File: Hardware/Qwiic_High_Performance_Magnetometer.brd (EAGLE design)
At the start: 25.4 x 25.4 mm, 46 parts, among them J1 Qwiic, J2 Qwiic, U1 MMC5893MA_QFN16

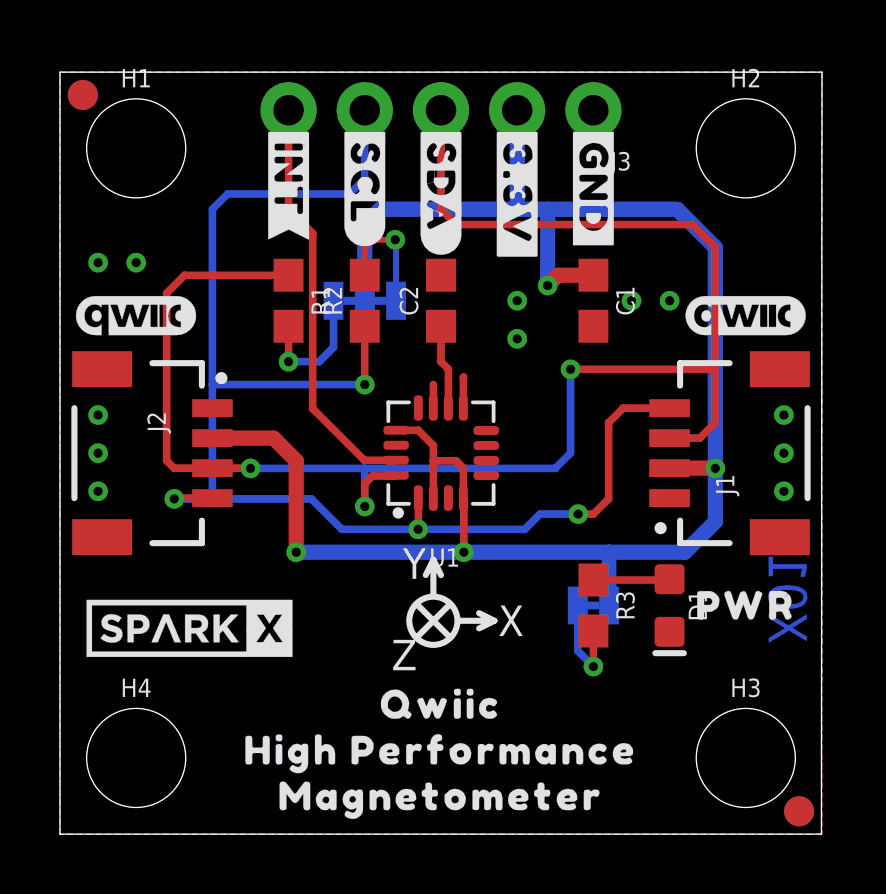
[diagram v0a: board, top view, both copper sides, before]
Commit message: Added SPI breakout header; created PCB production files.
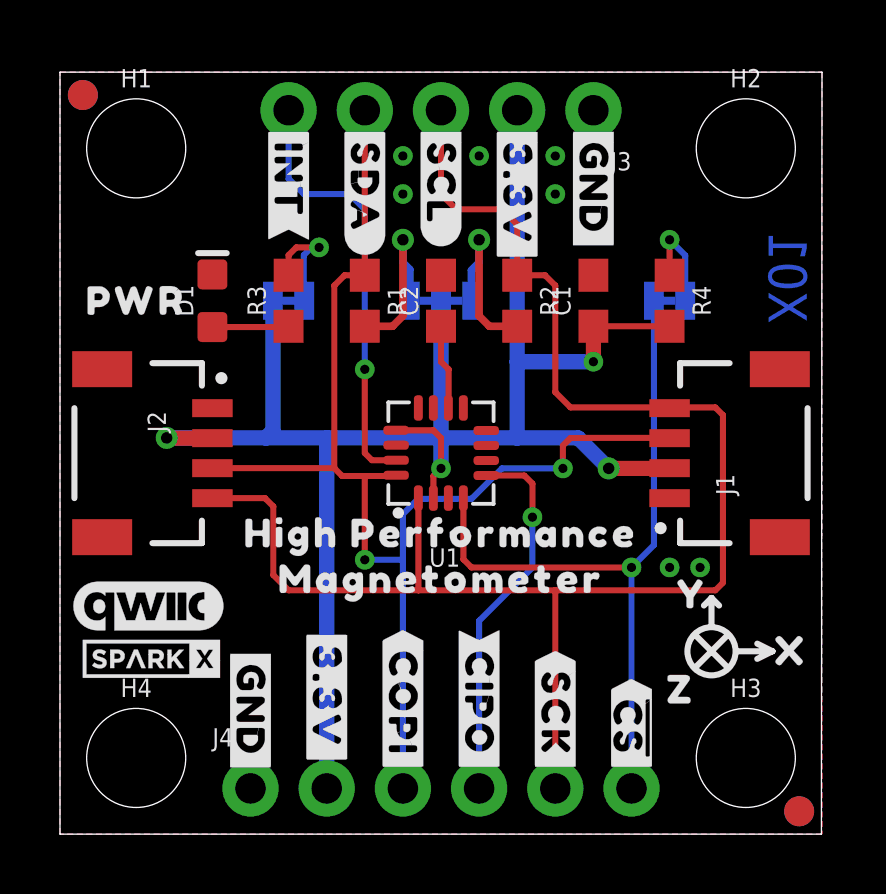
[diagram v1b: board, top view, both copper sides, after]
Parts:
- added J4: (no value), SparkFun-Connectors:1X06_NO_SILK
- added JP2: JUMPER-SMT_2_NC_TRACE_SILK, SparkFun-Jumpers:SMT-JUMPER_2_NC_TRACE_SILK
- added R4: 10k, SparkFun-Resistors:0603
- added U$23: (no value), output:#SPI#9
- added U$24: (no value), output:MAGNETOMETER12
- added U$25: (no value), output:X15
- added U$26: (no value), output:Y16
- added U$27, U$39: (no value), output:Z17
- added U$28: (no value), output:#GND#4
- added U$29: (no value), output:#3#3V#0
- added U$30: (no value), output:#COPI#12
- added U$31: (no value), output:#CIPO#11
- added U$32: (no value), output:#SCK#13
- added U$33: (no value), output:##CS##10
- added U$34: (no value), output:MADE_IN_THE_USA20
- added U$35: (no value), output:#SCL#6
- added U$36: SPARKX-LOGO2, SparkX:SPARKX-TINY
- added U$37: SPARKX-LOGO3, SparkX:SPARKX-SMALL
- added U$38: (no value), output:#SDA#5
- LOGO2, LOGO3: value QWIIC_LOGO_4MM -> QWIIC_LOGO_5MM; device SparkFun-Aesthetics:QWIIC_4MM -> SparkFun-Aesthetics:QWIIC_5MM
- U$1: value SPARKX-LOGO5 -> (none); device SparkX:SPARKX-LARGE -> output:HIGH_PERFORMANCE11
- U$14: device output:#SCL#6 -> output:#SCK#13
- U$15: device output:#SDA#5 -> output:##CS##10
- U$17: device output:MADE_IN_THE_USA13 -> output:#GND#4
- U$18: device output:QWIIC10 -> output:#3#3V#0
- U$19: device output:HIGH_PERFORMANCE11 -> output:Y16
- U$2: value SPARKX-LOGO3 -> (none); device SparkX:SPARKX-SMALL -> output:#SCL#6
- U$20: device output:MAGNETOMETER12 -> output:X15
- U$5: device output:#SCL#6 -> output:#SDA#5
- U$6: device output:#SDA#5 -> output:#CIPO#11
- U$9: device output:QWIIC10 -> output:#COPI#12
- moved U$14 22.7 mm to (16.5, 1.91), flipped to the top
- moved U$15 22.7 mm to (19.1, 1.91), flipped to the top
- moved U$8 22.7 mm to (2.54, 17.8)
- moved LOGO2 22.0 mm to (3.05, 7.62), flipped to the bottom
- moved U$6 21.9 mm to (14.0, 1.91)
- moved U$2 18.9 mm to (12.7, 23.7), turned to 270 degrees
- moved D1 18.3 mm to (5.08, 17.8), turned to 90 degrees
- moved JP3 14.4 mm to (7.62, 17.8), turned to 0 degrees
- moved R3 14.4 mm to (7.62, 17.8), turned to 90 degrees
- moved U$21 12.1 mm to (7.62, 16.0)
- moved U$20 12.1 mm to (24.4, 6.10), flipped to the top
- moved LOGO3 9.66 mm to (2.92, 7.62)
- moved U$19 9.16 mm to (21.1, 8.00), flipped to the top
- moved U$17 8.29 mm to (6.35, 6.35), flipped to the top, turned to 270 degrees
- moved U$11 7.24 mm to (12.7, 8.51)
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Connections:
- removed net SCL: J1.4, J2.4, J3.4, R2.1, U1.1
- removed net SDA: J1.3, J2.3, J3.3, R1.1, U1.16
- new net !CS!: J4.6, JP2.1, U1.4
- new net CIPO: J4.4, U1.5
- new net N$5: JP2.2, R4.1
- new net SCL/SCK: J1.4, J2.4, J3.3, J4.5, R2.1, U1.1
- new net SDA/COPI: J1.3, J2.3, J3.4, J4.3, R1.1, U1.16
- net 3.3V: now also J4.2, R4.2; no longer U1.4
- net GND: now also J4.1
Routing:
- net SDA: track 55.0 -> 0.00 mm, vias 3 -> 0
- net SCL/SCK: track 0.00 -> 53.4 mm
- net SCL: track 46.9 -> 0.00 mm, vias 4 -> 0
- net SDA/COPI: track 0.00 -> 42.6 mm, vias 0 -> 2
- net !CS!: track 0.00 -> 24.3 mm, vias 0 -> 1
- net CIPO: track 0.00 -> 12.5 mm, vias 0 -> 1
- net N$5: track 0.00 -> 3.43 mm, vias 0 -> 1
- net N$2: track 4.09 -> 6.10 mm
- net GND: track 1.82 -> 0.00 mm, vias 12 -> 7
- net N$3: track 4.43 -> 6.08 mm
- net 3.3V: track 62.6 -> 61.6 mm
- net INT: track 13.8 -> 14.5 mm, vias 0 -> 1
- net N$1: track 3.43 -> 3.94 mm
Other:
- board text removed: "X"
- board text removed: "Y"
- board text removed: "Z"

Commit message: Fixed SPI header alignment.
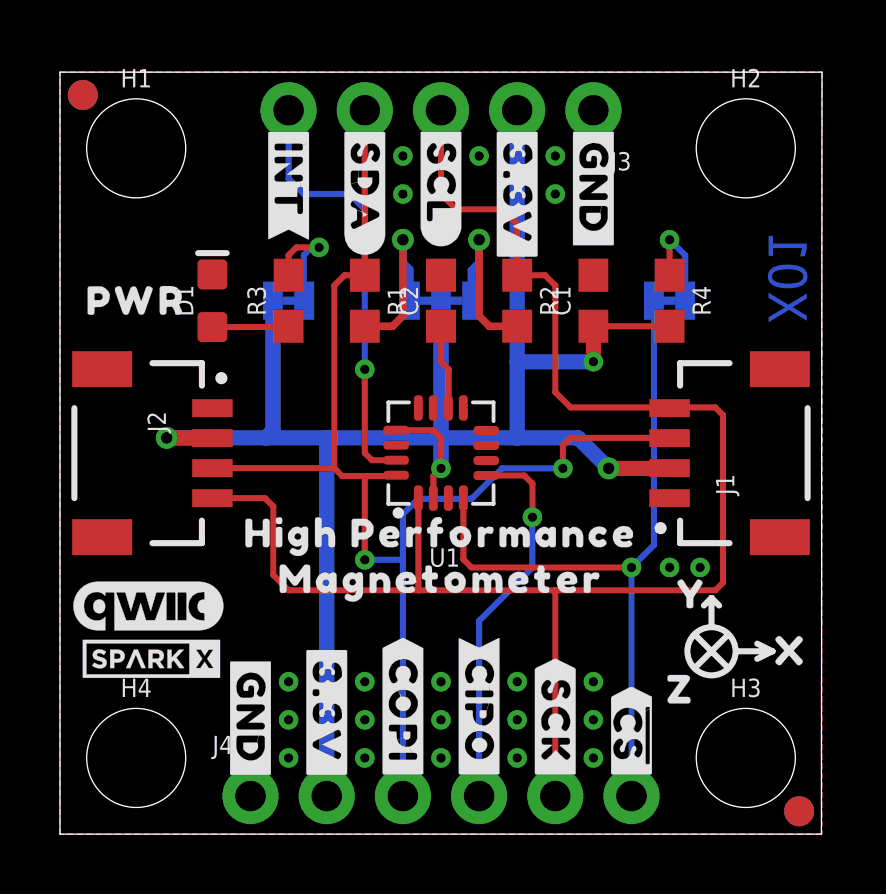
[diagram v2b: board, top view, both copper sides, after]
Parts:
- moved U$18 0.51 mm to (8.89, 6.48)
- moved J4 0.25 mm to (6.35, 1.27)
- moved U$14 0.25 mm to (16.5, 1.65)
- moved U$15 0.25 mm to (19.1, 1.65)
- moved U$30 0.25 mm to (11.4, 1.65)
- moved U$31 0.25 mm to (14.0, 1.65)
- moved U$32 0.25 mm to (16.5, 1.65)
- moved U$33 0.25 mm to (19.1, 1.65)
- moved U$6 0.25 mm to (14.0, 1.65)
- moved U$9 0.25 mm to (11.4, 1.65)
- moved U$17 0.25 mm to (6.35, 6.10)
- moved U$28 0.25 mm to (6.35, 6.10)
- moved U$29 0.25 mm to (8.89, 6.48)

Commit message: Improved top ground plane under the IC.
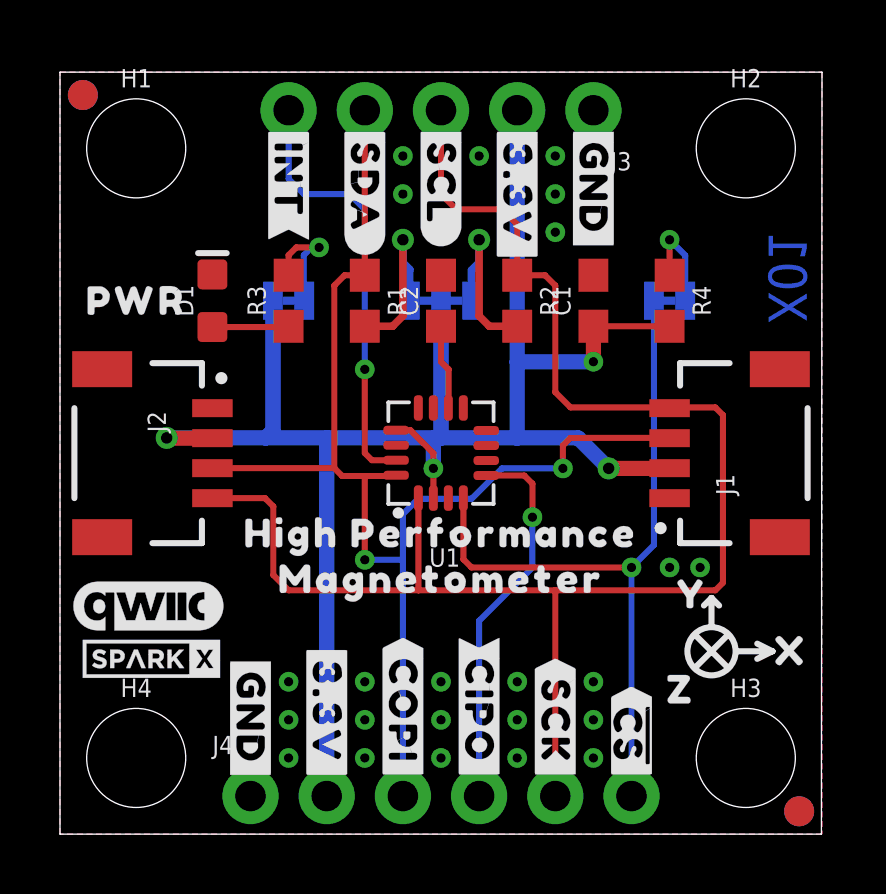
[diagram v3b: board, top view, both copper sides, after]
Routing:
- net 3.3V: track 61.8 -> 61.2 mm
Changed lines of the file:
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@@
 <drawing>
 <settings>
-<setting alwaysvectorfont="yes"/>
+<setting alwaysvectorfont="no"/>
 <setting verticaltext="up"/>
 </settings>
-<grid distance="0.05" unitdist="inch" unit="inch" style="lines" multiple="1" display="yes" altdistance="0.005" altunitdist="inch" altunit="inch"/>
+<grid distance="0.01" unitdist="inch" unit="inch" style="lines" multiple="1" display="yes" altdistance="0.005" altunitdist="inch" altunit="inch"/>
 <layers>
 <layer number="1" name="Top" color="4" fill="1" visible="yes" active="yes"/>
@@
 <layer number="23" name="tOrigins" color="15" fill="1" visible="yes" active="yes"/>
 <layer number="24" name="bOrigins" color="15" fill="1" visible="yes" active="yes"/>
-<layer number="25" name="tNames" color="7" fill="1" visible="yes" active="yes"/>
-<layer number="26" name="bNames" color="7" fill="1" visible="yes" active="yes"/>
-<layer number="27" name="tValues" color="7" fill="1" visible="yes" active="yes"/>
-<layer number="28" name="bValues" color="7" fill="1" visible="yes" active="yes"/>
-<layer number="29" name="tStop" color="7" fill="3" visible="yes" active="yes"/>
-<layer number="30" name="bStop" color="7" fill="6" visible="yes" active="yes"/>
-<layer number="31" name="tCream" color="7" fill="4" visible="yes" active="yes"/>
-<layer number="32" name="bCream" color="7" fill="5" visible="yes" active="yes"/>
-<layer number="33" name="tFinish" color="6" fill="3" visible="yes" active="yes"/>
-<layer number="34" name="bFinish" color="6" fill="6" visible="yes" active="yes"/>
-<layer number="35" name="tGlue" color="7" fill="4" visible="yes" active="yes"/>
-<layer number="36" name="bGlue" color="7" fill="5" visible="yes" active="yes"/>
-<layer number="37" name="tTest" color="7" fill="1" visible="yes" active="yes"/>
-<layer number="38" name="bTest" color="7" fill="1" visible="yes" active="yes"/>
-<layer number="39" name="tKeepout" color="4" fill="11" visible="yes" active="yes"/>
-<layer number="40" name="bKeepout" color="1" fill="11" visible="yes" active="yes"/>
-<layer number="41" name="tRestrict" color="4" fill="10" visible="yes" active="yes"/>
-<layer number="42" name="bRestrict" color="1" fill="10" visible="yes" active="yes"/>
-<layer number="43" name="vRestrict" color="2" fill="10" visible="yes" active="yes"/>
-<layer number="44" name="Drills" color="7" fill="1" visible="yes" active="yes"/>
+<layer number="25" name="tNames" color="7" fill="1" visible="no" active="yes"/>
+<layer number="26" name="bNames" color="7" fill="1" visible="no" active="yes"/>
+<layer number="27" name="tValues" color="7" fill="1" visible="no" active="yes"/>
+<layer number="28" name="bValues" color="7" fill="1" visible="no" active="yes"/>
+<layer number="29" name="tStop" color="7" fill="3" visible="no" active="yes"/>
+<layer number="30" name="bStop" color="7" fill="6" visible="no" active="yes"/>
+<layer number="31" name="tCream" color="7" fill="4" visible="no" active="yes"/>
+<layer number="32" name="bCream" color="7" fill="5" visible="no" active="yes"/>
+<layer number="33" name="tFinish" color="6" fill="3" visible="no" active="yes"/>
+<layer number="34" name="bFinish" color="6" fill="6" visible="no" active="yes"/>
+<layer number="35" name="tGlue" color="7" fill="4" visible="no" active="yes"/>
+<layer number="36" name="bGlue" color="7" fill="5" visible="no" active="yes"/>
+<layer number="37" name="tTest" color="7" fill="1" visible="no" active="yes"/>
+<layer number="38" name="bTest" color="7" fill="1" visible="no" active="yes"/>
+<layer number="39" name="tKeepout" color="4" fill="11" visible="no" active="yes"/>
+<layer number="40" name="bKeepout" color="1" fill="11" visible="no" active="yes"/>
+<layer number="41" name="tRestrict" color="4" fill="10" visible="no" active="yes"/>
+<layer number="42" name="bRestrict" color="1" fill="10" visible="no" active="yes"/>
+<layer number="43" name="vRestrict" color="2" fill="10" visible="no" active="yes"/>
+<layer number="44" name="Drills" color="7" fill="1" visible="no" active="yes"/>
 <layer number="45" name="Holes" color="7" fill="1" visible="yes" active="yes"/>
-<layer number="46" name="Milling" color="3" fill="1" visible="yes" active="yes"/>
-<layer number="47" name="Measures" color="7" fill="1" visible="yes" active="yes"/>
-<layer number="48" name="Document" color="7" fill="1" visible="yes" active="yes"/>
-<layer number="49" name="Reference" color="7" fill="1" visible="yes" active="yes"/>
+<layer number="46" name="Milling" color="3" fill="1" visible="no" active="yes"/>
+<layer number="47" name="Measures" color="7" fill="1" visible="no" active="yes"/>
+<layer number="48" name="Document" color="7" fill="1" visible="no" active="yes"/>
+<layer number="49" name="Reference" color="7" fill="1" visible="no" active="yes"/>
 <layer number="50" name="dxf" color="7" fill="1" visible="no" active="no"/>
 <layer number="51" name="tDocu" color="6" fill="1" visible="yes" active="yes"/>
-<layer number="52" name="bDocu" color="7" fill="1" visible="yes" active="yes"/>
+<layer number="52" name="bDocu" color="7" fill="1" visible="no" active="yes"/>
 <layer number="53" name="tGND_GNDA" color="7" fill="9" visible="no" active="no"/>
 <layer number="54" name="bGND_GNDA" color="1" fill="9" visible="no" active="no"/>
@@
 <via x="15.24" y="5.08" extent="1-16" drill="0.3048"/>
 <via x="15.24" y="2.54" extent="1-16" drill="0.3048"/>
+<via x="16.51" y="20.066" extent="1-16" drill="0.3048"/>
 </signal>
 <signal name="3.3V">
@@
 <wire x1="3.556" y1="13.208" x2="6.858" y2="13.208" width="0.508" layer="16"/>
 <wire x1="6.858" y1="13.208" x2="8.89" y2="13.208" width="0.508" layer="16"/>
-<wire x1="8.89" y1="13.208" x2="12.7" y2="13.208" width="0.508" layer="16"/>
+<wire x1="8.89" y1="13.208" x2="12.446" y2="13.208" width="0.508" layer="16"/>
+<wire x1="12.446" y1="13.208" x2="12.7" y2="13.208" width="0.508" layer="16"/>
 <wire x1="12.7" y1="13.208" x2="15.24" y2="13.208" width="0.508" layer="16"/>
 <wire x1="15.24" y1="13.208" x2="17.272" y2="13.208" width="0.508" layer="16"/>
@@
 <wire x1="7.0993" y1="17.78" x2="7.0993" y2="13.4493" width="0.508" layer="16"/>
 <wire x1="7.0993" y1="13.4493" x2="6.858" y2="13.208" width="0.508" layer="16"/>
-<wire x1="12.446" y1="11.202" x2="12.446" y2="11.938" width="0.2032" layer="1"/>
-<wire x1="12.446" y1="11.938" x2="12.7" y2="12.192" width="0.2032" layer="1"/>
-<via x="12.7" y="12.192" extent="1-16" drill="0.3048"/>
-<wire x1="11.204" y1="13.464" x2="12.444" y2="13.464" width="0.2032" layer="1"/>
-<wire x1="12.444" y1="13.464" x2="12.7" y2="13.208" width="0.2032" layer="1"/>
-<wire x1="12.7" y1="13.208" x2="12.7" y2="12.192" width="0.2032" layer="1"/>
-<wire x1="12.7" y1="12.192" x2="12.7" y2="13.208" width="0.508" layer="16"/>
+<wire x1="12.446" y1="11.202" x2="12.446" y2="12.192" width="0.2032" layer="1"/>
+<via x="12.446" y="12.192" extent="1-16" drill="0.3048"/>
+<wire x1="12.446" y1="12.192" x2="12.446" y2="13.208" width="0.508" layer="16"/>
+<wire x1="11.204" y1="13.464" x2="11.682" y2="13.464" width="0.2032" layer="1"/>
+<wire x1="12.446" y1="12.7" x2="12.446" y2="12.192" width="0.2032" layer="1"/>
+<wire x1="11.682" y1="13.464" x2="12.446" y2="12.7" width="0.2032" layer="1"/>
 </signal>
 <signal name="N$1">
